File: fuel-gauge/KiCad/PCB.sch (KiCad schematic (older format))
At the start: 39 parts, among them P1 CONN_01X04, P2 CONN_01X04, P3 CONN_01X04, Q1 BSS84, Q2 BSS138, Q3 2N7002, SW1 Switch_SPDT_x2, U1 AQV252G, U2 SN74LVC1G08DBVR, U3 TLV3691IDCKR, U4 bq34z100pw

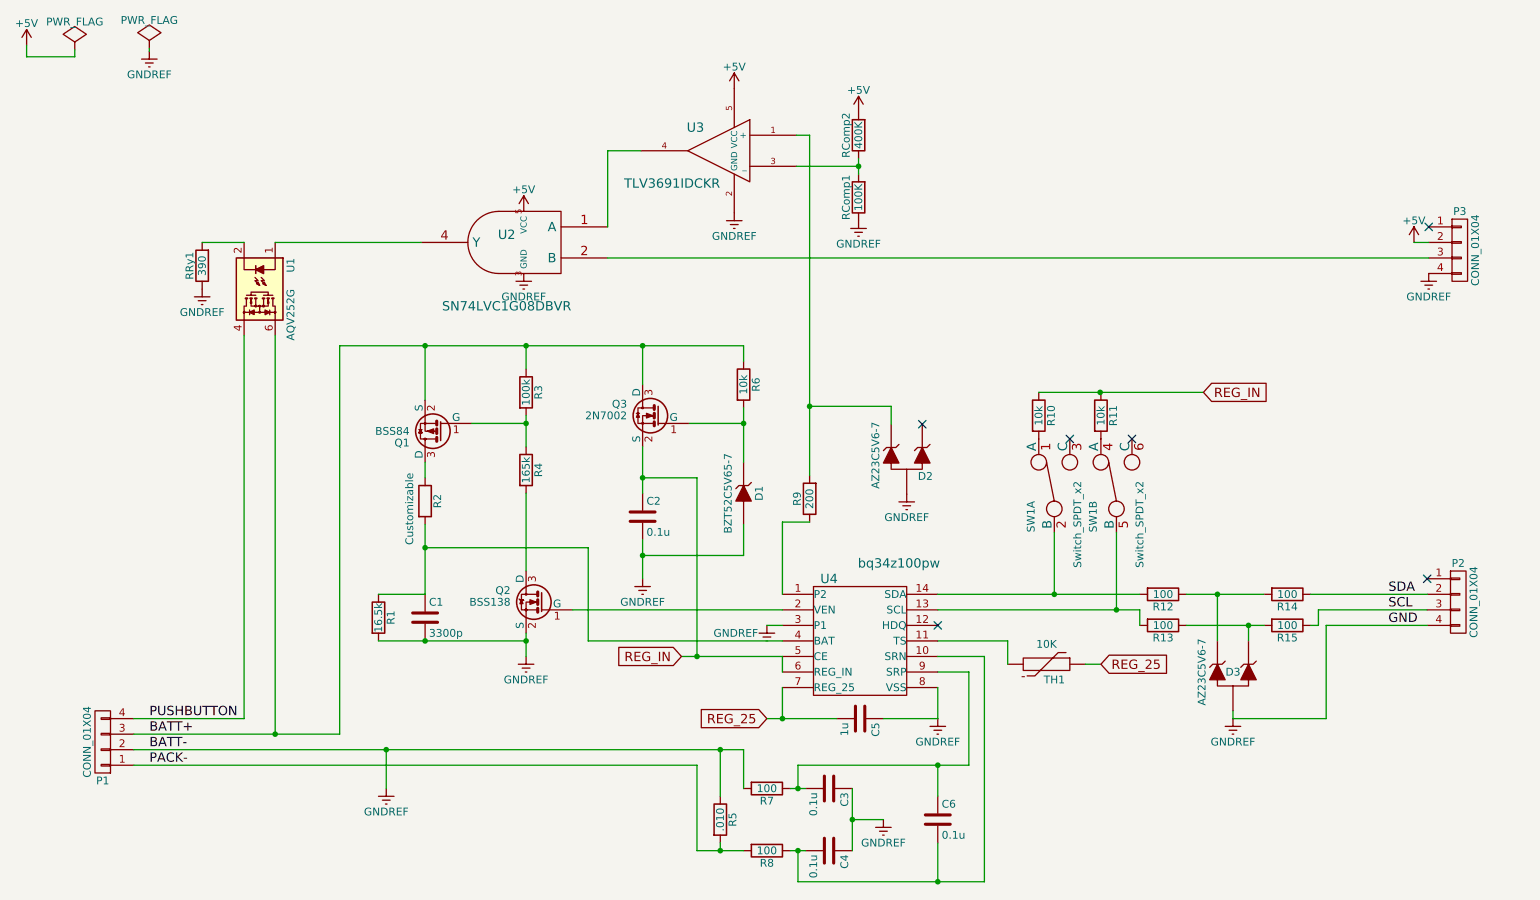
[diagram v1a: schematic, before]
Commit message: Update the design to the v2
Include new routing to minimize the number of vias used and some
electrical considerations. Also the names of the connectors and the
positions of the switch.
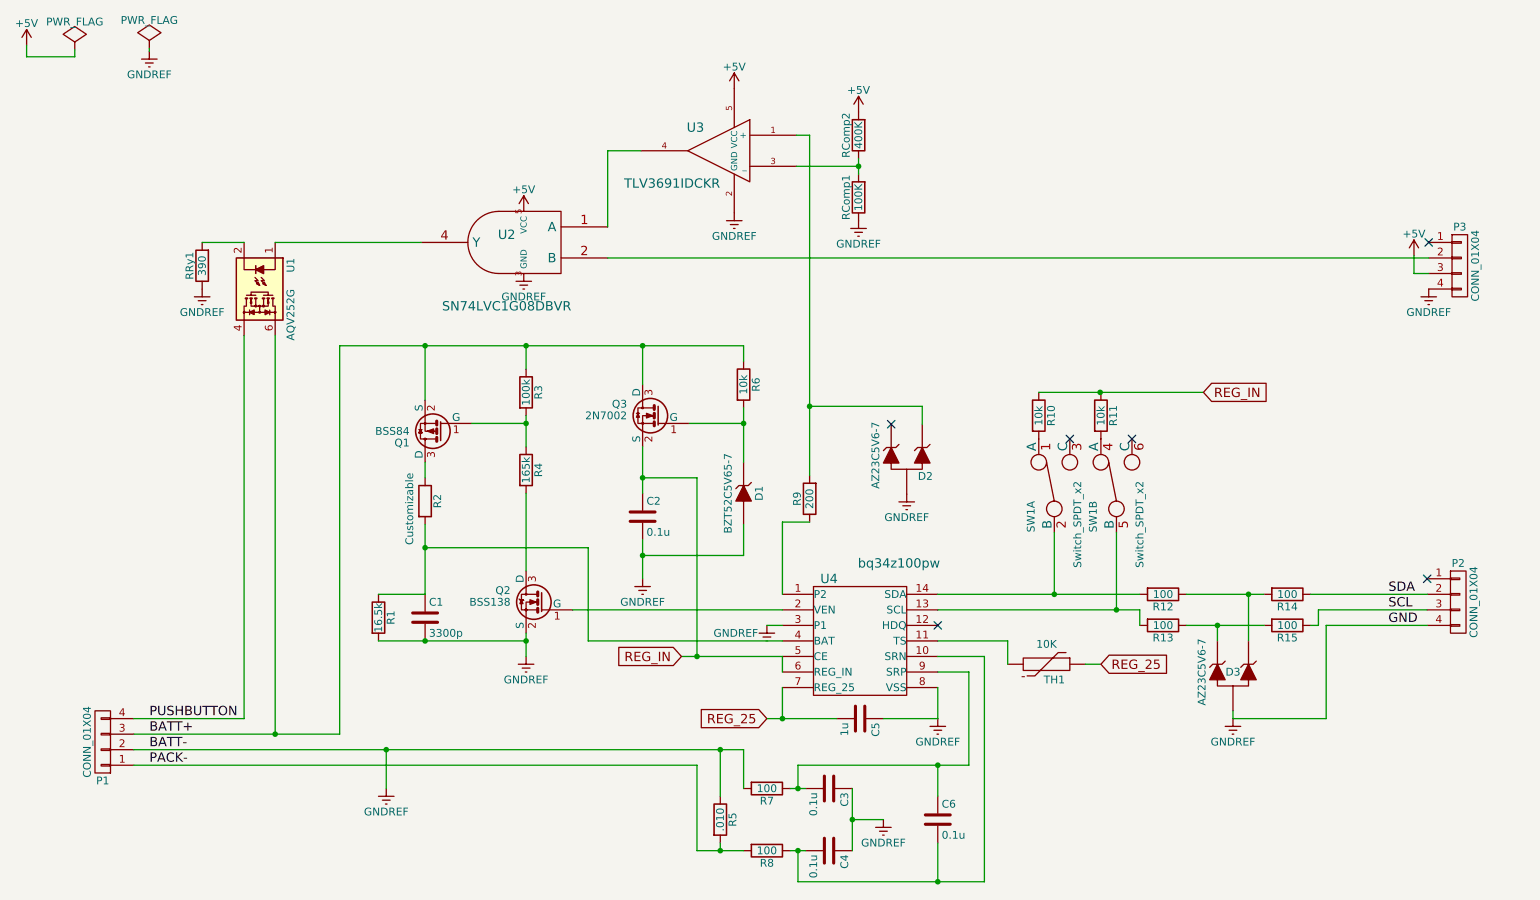
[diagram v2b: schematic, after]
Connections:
- net +5V: now also P3.3 (P3); no longer P3.2 (P2)
- net at R12.1, R14.2: now also D3.2 (K); no longer D3.1 (K)
- net at R13.1, R15.2: now also D3.1 (K); no longer D3.2 (K)
- net at U2.2 (B): now also P3.2 (P2); no longer P3.3 (P3)
- net at R9.2, U3.1 (+): now also D2.2 (K); no longer D2.1 (K)
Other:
- moved on the sheet: P3

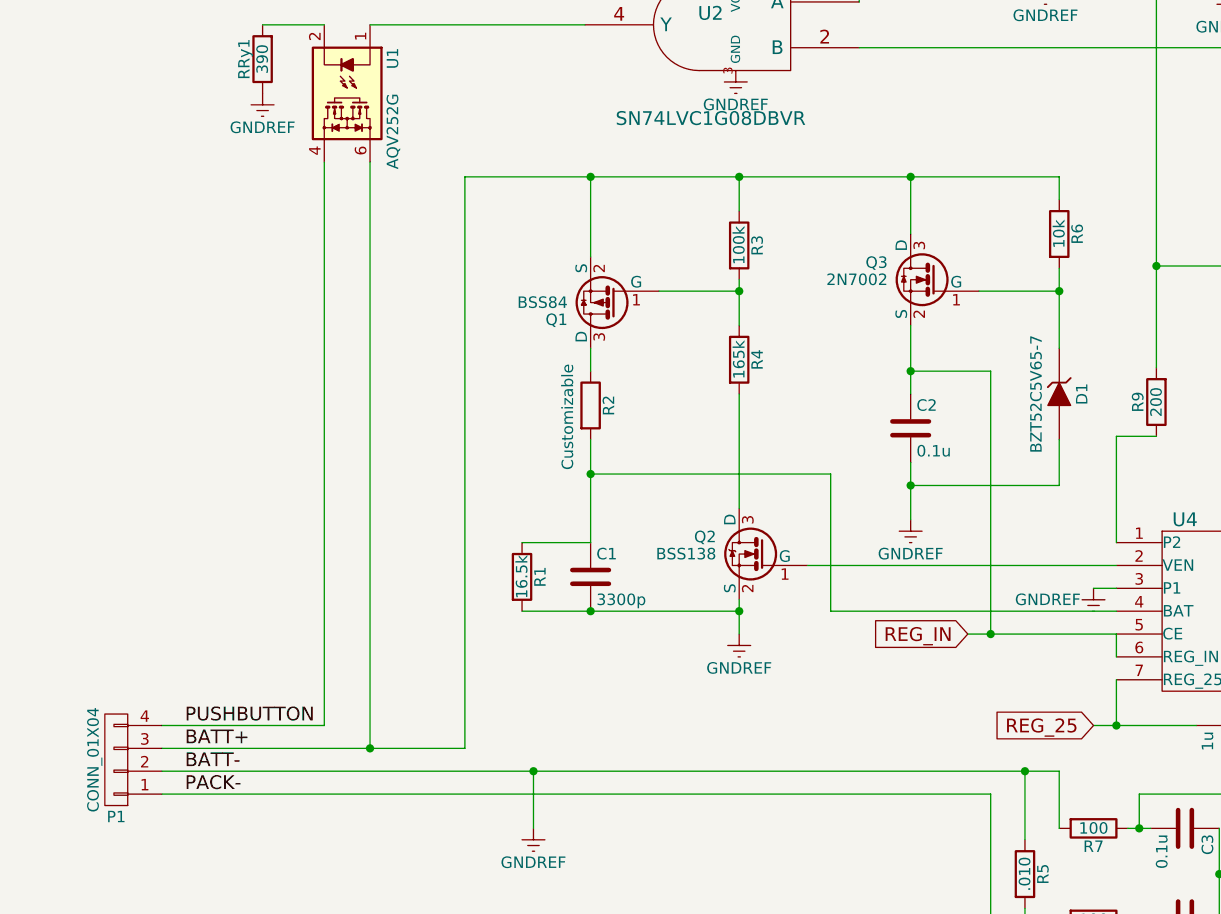
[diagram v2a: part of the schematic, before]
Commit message: Modify the circuit in order to fit with the UGV v2.0 wiring
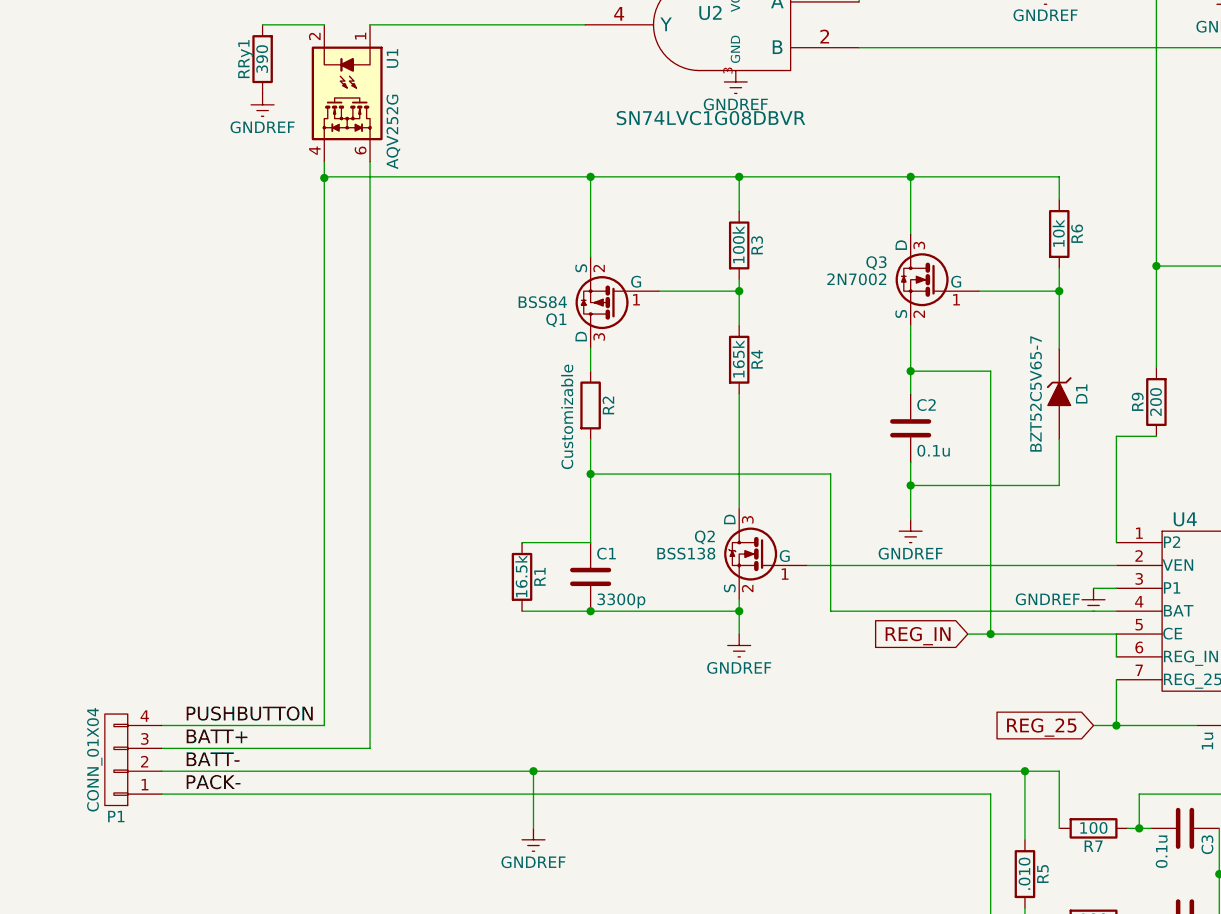
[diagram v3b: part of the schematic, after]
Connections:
- net BATT+: no longer Q1.2 (S), Q3.3 (D), R3.1, R6.1
- net PUSHBUTTON: now also Q1.2 (S), Q3.3 (D), R3.1, R6.1
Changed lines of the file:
@@
 	2360 2640 2360 5205
 Wire Wire Line
-	2160 5105 2160 2640
-Connection ~ 2360 5205
-Wire Wire Line
-	1450 5105 2160 5105
+	2160 2640 2160 5105
+Wire Wire Line
+	2160 5105 1450 5105
 Connection ~ 5800 3095
 Wire Wire Line
@@
 	5625 4605 4375 4605
 Wire Wire Line
-	1450 5205 2775 5205
-Wire Wire Line
-	2775 5205 2775 2705
+	2360 5205 1450 5205
 Connection ~ 5225 5955
 Wire Wire Line
@@
 	3325 3055 3325 2705
 Wire Wire Line
-	2775 2705 5375 2705
+	2160 2705 5375 2705
 Wire Wire Line
 	3975 2705 3975 2855
@@
 	9690 2240 9690 2125
 NoConn ~ 9785 2040
+Wire Wire Line
+	2160 2705 2160 2710
+Connection ~ 2160 2710
 $EndSCHEMATC

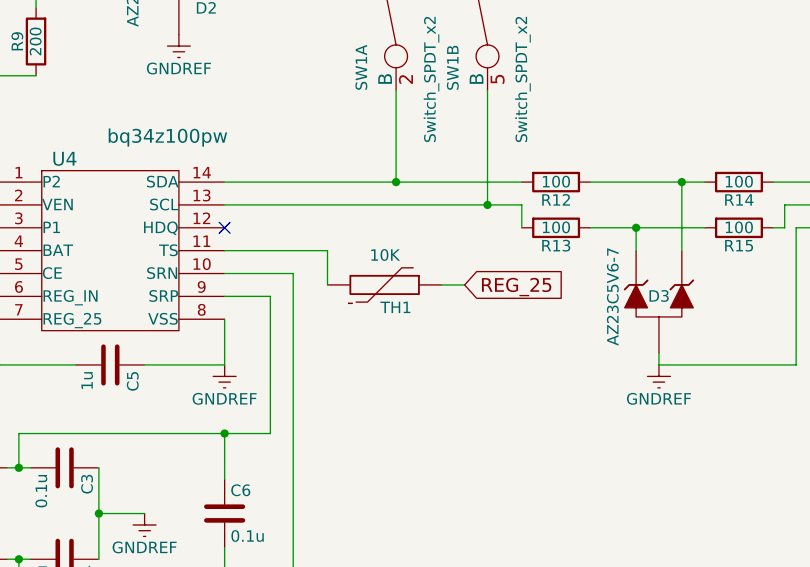
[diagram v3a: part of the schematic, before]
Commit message: Change a component and redesign drills
The thermistor is sustituted by a connector in order to have no wirings
in the PCB. The thermistor has to be located near the battery.

Drills were redesign in orther to create a correct version to send to a
PCB manufacturer.
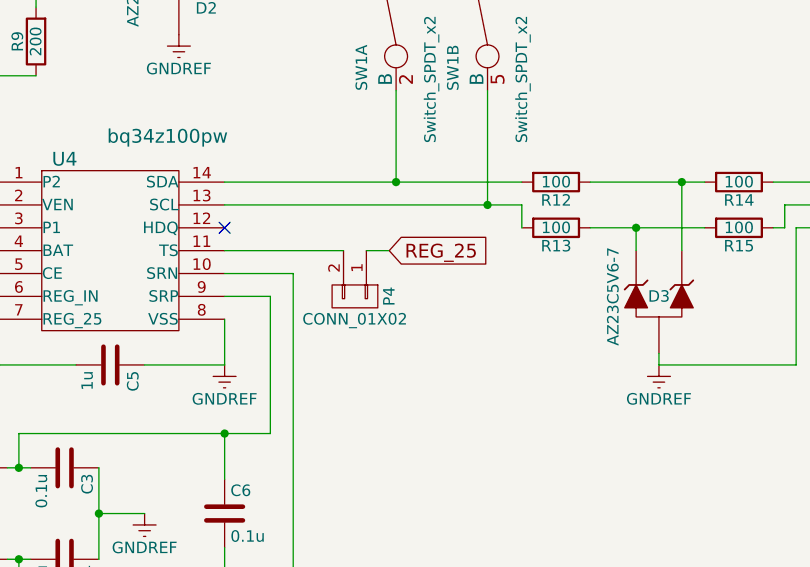
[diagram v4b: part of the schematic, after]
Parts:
- removed TH1: 10K, footprint:Thermistor, symbol THERMISTOR
- added P4: CONN_01X02, footprint:CONN_01X02, symbol CONN_01X02
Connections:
- net REG_25: now also P4.1 (P1)
- net at U4.11 (TS): now also P4.2 (P2)
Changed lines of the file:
@@
 Text GLabel 4975 4705 0    60   Input ~ 0
 REG_IN
-$Comp
-L THERMISTOR TH1
-U 1 1 59163373
-P 7325 4755
-F 0 "TH1" V 7425 4805 50  0000 C CNN
-F 1 "10K" V 7225 4755 50  0000 C BNN
-F 2 "footprint:Thermistor" H 7325 4755 60  0001 C CNN
-F 3 "" H 7325 4755 60  0000 C CNN
-	1    7325 4755
-	0    1    1    0
-$EndComp
 Text GLabel 5525 5105 0    60   Input ~ 0
 REG_25
-Text GLabel 7675 4755 2    60   Input ~ 0
+Text GLabel 7345 4605 2    60   Input ~ 0
 REG_25
 Text Label 9525 4305 0    60   ~ 0
@@
 	5375 5305 5375 5555
 Wire Wire Line
-	7675 4755 7575 4755
+	7345 4605 7245 4605
 Connection ~ 5625 5105
 Wire Wire Line
-	7075 4605 6625 4605
-Wire Wire Line
-	7075 4755 7075 4605
+	6625 4605 7145 4605
 Connection ~ 5075 4705
 Wire Wire Line
@@
 	2160 2705 2160 2710
 Connection ~ 2160 2710
+$Comp
+L CONN_01X02 P4
+U 1 1 5A0C89B9
+P 7195 4805
+F 0 "P4" H 7195 4955 50  0000 C CNN
+F 1 "CONN_01X02" V 7295 4805 50  0000 C CNN
+F 2 "footprint:CONN_01X02" H 7195 4805 60  0001 C CNN
+F 3 "" H 7195 4805 60  0000 C CNN
+	1    7195 4805
+	0    1    1    0
+$EndComp
 $EndSCHEMATC

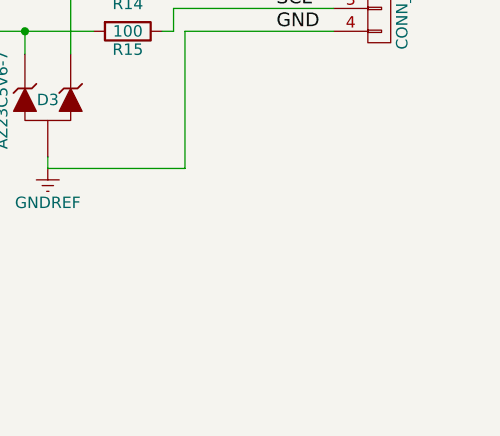
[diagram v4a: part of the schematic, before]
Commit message: Update the v2.0 of the fuel gauge PCB
Include the Bill of Materials (BOM) with all the components

Include the new footprint of the mounting hole
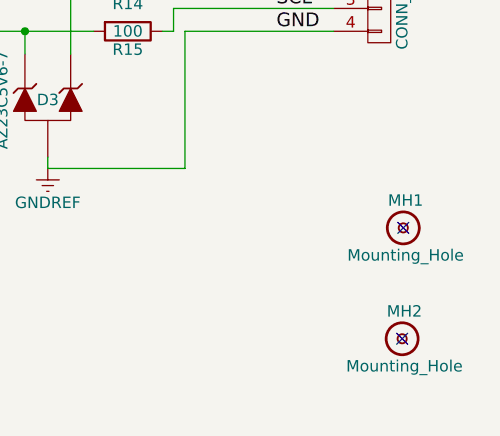
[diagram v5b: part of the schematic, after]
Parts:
- added MH1, MH2: Mounting_Hole, footprint:Mounting_hole, symbol Mounting_Hole
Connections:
- no-connect marks 6 -> 8
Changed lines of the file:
@@
 	0    1    1    0
 $EndComp
+$Comp
+L Mounting_Hole MH1
+U 1 1 5A12BF39
+P 10080 5365
+F 0 "MH1" H 10090 5485 50  0000 C CNN
+F 1 "Mounting_Hole" H 10090 5245 50  0000 C CNN
+F 2 "footprint:Mounting_hole" H 10080 5365 60  0001 C CNN
+F 3 "" H 10080 5365 60  0000 C CNN
+	1    10080 5365
+	1    0    0    -1
+$EndComp
+$Comp
+L Mounting_Hole MH2
+U 1 1 5A12C489
+P 10075 5850
+F 0 "MH2" H 10085 5970 50  0000 C CNN
+F 1 "Mounting_Hole" H 10085 5730 50  0000 C CNN
+F 2 "footprint:Mounting_hole" H 10075 5850 60  0001 C CNN
+F 3 "" H 10075 5850 60  0000 C CNN
+	1    10075 5850
+	1    0    0    -1
+$EndComp
+NoConn ~ 10080 5365
+NoConn ~ 10075 5850
 $EndSCHEMATC
